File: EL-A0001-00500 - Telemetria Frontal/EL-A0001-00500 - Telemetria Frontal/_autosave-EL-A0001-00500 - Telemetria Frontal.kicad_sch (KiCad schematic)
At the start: 3 parts, among them J1 1-776087-1, U1 YAAJ_BluePill, U2 MP1584

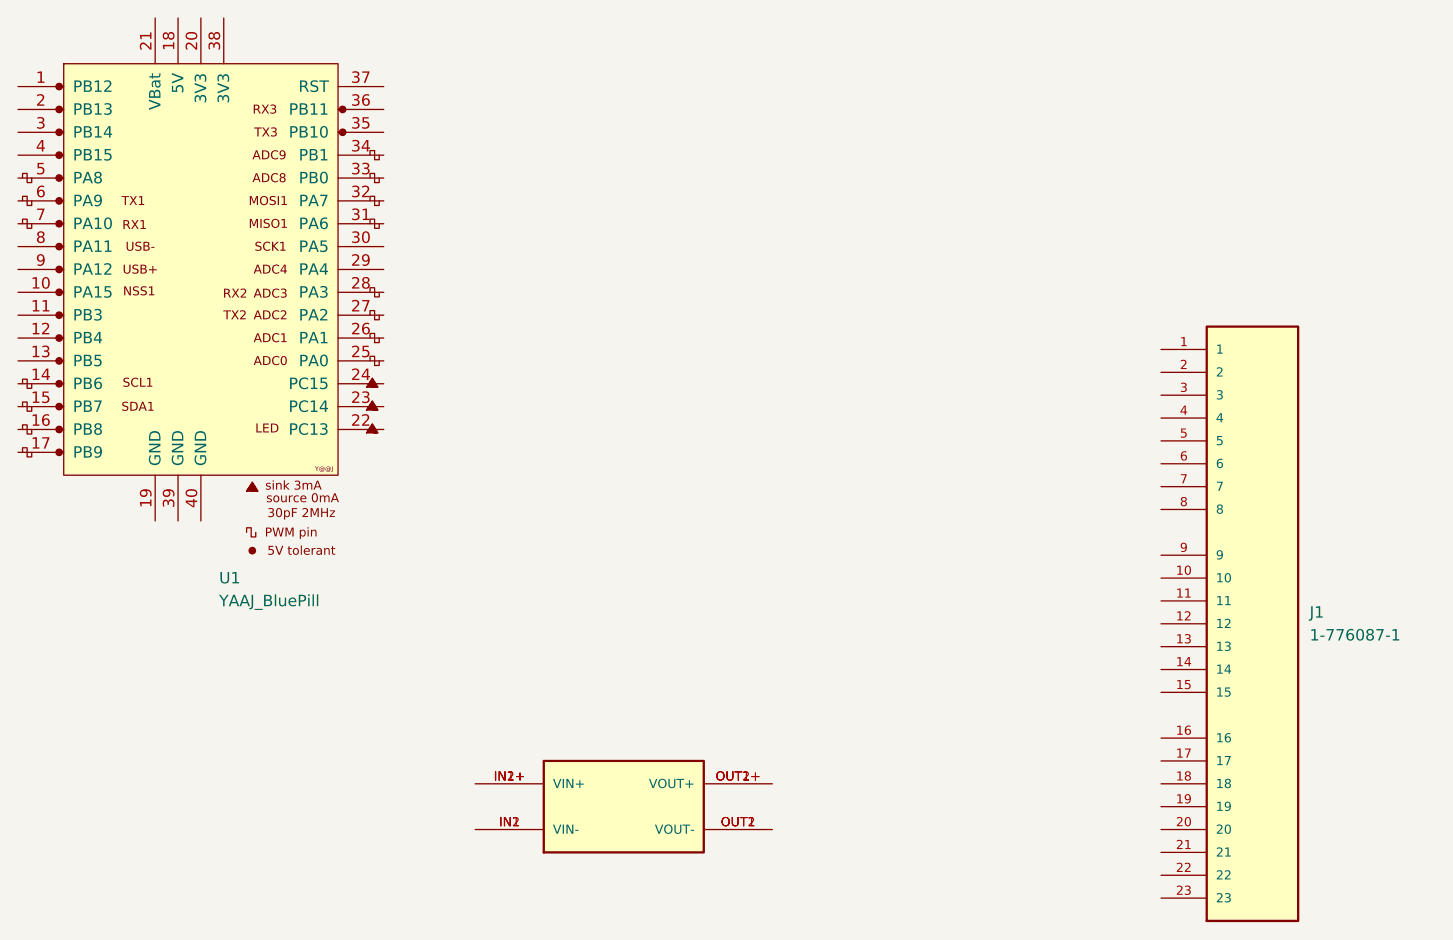
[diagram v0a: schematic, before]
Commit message: ADD: submodules
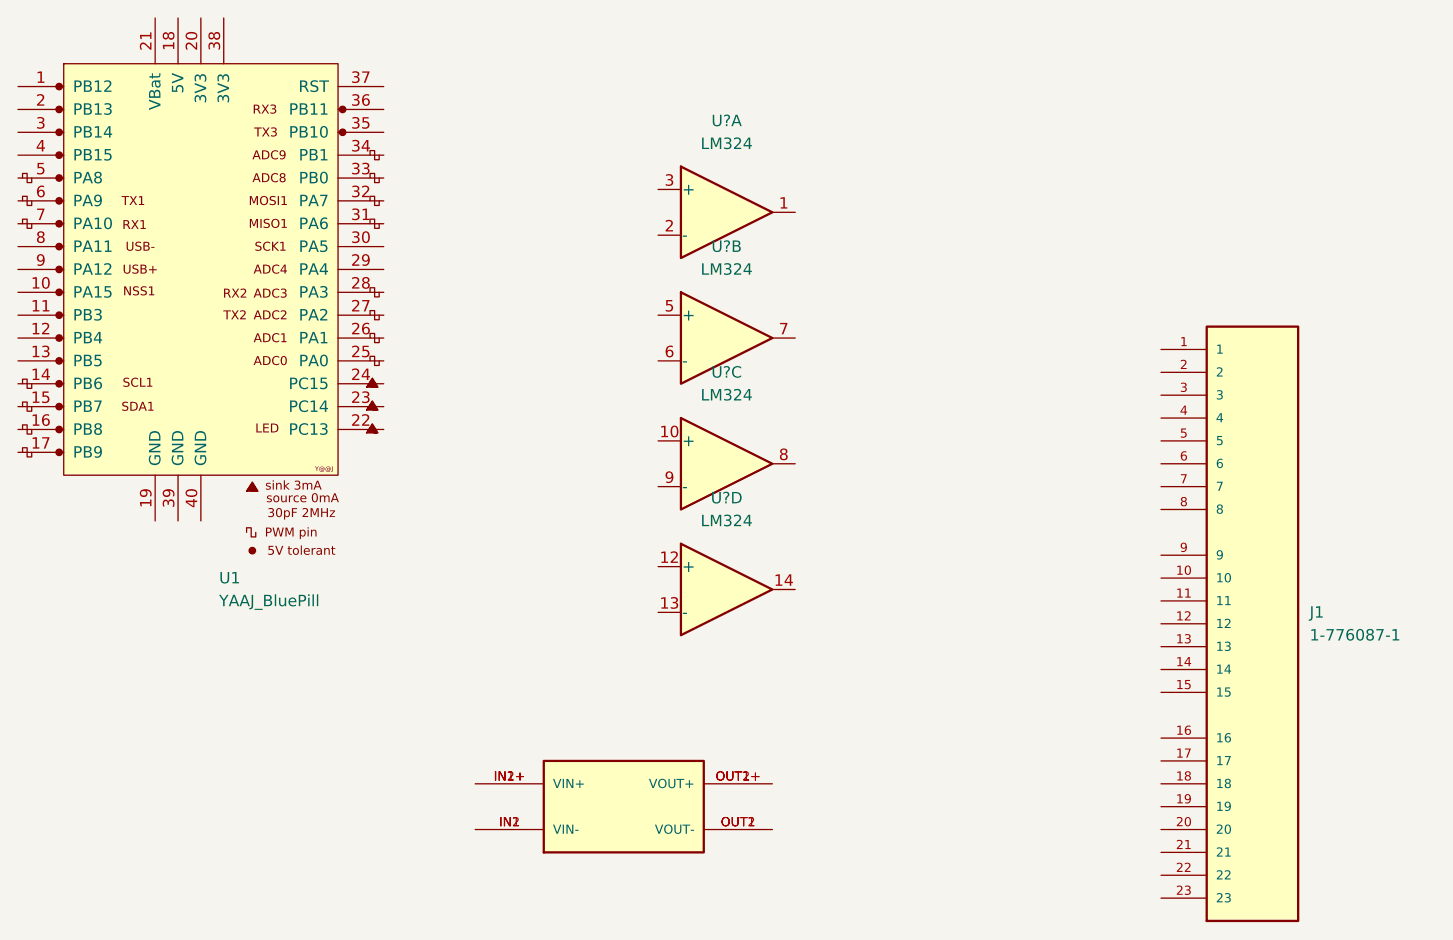
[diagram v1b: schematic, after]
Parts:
- added U? (x4): LM324, symbol Amplifier_Operational:LM324
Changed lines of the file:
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@@
 (kicad_sch (version 20211123) (generator eeschema)
   (paper "A4")
+  (symbol (lib_id "Amplifier_Operational:LM324") (at 124.46 57.15 0) (unit 1)
+    (in_bom yes) (on_board yes) (fields_autoplaced)
+    (property "Reference" "U?" (id 0) (at 124.46 46.99 0))
+    (property "Value" "LM324" (id 1) (at 124.46 49.53 0))
+    (property "Footprint" "" (id 2) (at 123.19 54.61 0)
+      (effects (font (size 1.27 1.27)) hide)
+    )
+    (property "Datasheet" "http://www.ti.com/lit/ds/symlink/lm2902-n.pdf" (id 3) (at 125.73 52.07 0)
+      (effects (font (size 1.27 1.27)) hide)
+    )
+    (pin "1")
+    (pin "2")
+    (pin "3")
+  )
   (symbol (lib_id "1-776087-1:1-776087-1") (at 182.88 102.87 0) (unit 1)
     (in_bom yes) (on_board yes) (fields_autoplaced)
@@
     (pin "9")
   )
+  (symbol (lib_id "Amplifier_Operational:LM324") (at 124.46 71.12 0) (unit 2)
+    (in_bom yes) (on_board yes) (fields_autoplaced)
+    (property "Reference" "U?" (id 0) (at 124.46 60.96 0))
+    (property "Value" "LM324" (id 1) (at 124.46 63.5 0))
+    (property "Footprint" "" (id 2) (at 123.19 68.58 0)
+      (effects (font (size 1.27 1.27)) hide)
+    )
+    (property "Datasheet" "http://www.ti.com/lit/ds/symlink/lm2902-n.pdf" (id 3) (at 125.73 66.04 0)
+      (effects (font (size 1.27 1.27)) hide)
+    )
+    (pin "5")
+    (pin "6")
+    (pin "7")
+  )
+  (symbol (lib_id "Amplifier_Operational:LM324") (at 124.46 85.09 0) (unit 3)
+    (in_bom yes) (on_board yes) (fields_autoplaced)
+    (property "Reference" "U?" (id 0) (at 124.46 74.93 0))
+    (property "Value" "LM324" (id 1) (at 124.46 77.47 0))
+    (property "Footprint" "" (id 2) (at 123.19 82.55 0)
+      (effects (font (size 1.27 1.27)) hide)
+    )
+    (property "Datasheet" "http://www.ti.com/lit/ds/symlink/lm2902-n.pdf" (id 3) (at 125.73 80.01 0)
+      (effects (font (size 1.27 1.27)) hide)
+    )
+    (pin "10")
+    (pin "8")
+    (pin "9")
+  )
+  (symbol (lib_id "Amplifier_Operational:LM324") (at 124.46 99.06 0) (unit 4)
+    (in_bom yes) (on_board yes) (fields_autoplaced)
+    (property "Reference" "U?" (id 0) (at 124.46 88.9 0))
+    (property "Value" "LM324" (id 1) (at 124.46 91.44 0))
+    (property "Footprint" "" (id 2) (at 123.19 96.52 0)
+      (effects (font (size 1.27 1.27)) hide)
+    )
+    (property "Datasheet" "http://www.ti.com/lit/ds/symlink/lm2902-n.pdf" (id 3) (at 125.73 93.98 0)
+      (effects (font (size 1.27 1.27)) hide)
+    )
+    (pin "12")
+    (pin "13")
+    (pin "14")
+  )
   (symbol (lib_id "MP1584:MP1584") (at 111.76 123.19 0) (unit 1)
     (in_bom yes) (on_board yes) (fields_autoplaced)
@@
       (reference "U2") (unit 1) (value "MP1584") (footprint "MP1584:DC-BRICK")
     )
-  )
+    (path "/2aff3e19-72c1-4135-a3b2-de43d3a56a9c"
+      (reference "U?") (unit 1) (value "LM324") (footprint "")
+    )
+    (path "/ba775785-8bac-465f-9c4f-420dafb11e9d"
+      (reference "U?") (unit 2) (value "LM324") (footprint "")
+    )
+    (path "/c0fe2b63-3553-4f3d-b46a-4fab52b073bc"
+      (reference "U?") (unit 3) (value "LM324") (footprint "")
+    )
+    (path "/c284f113-28dd-4073-a844-cc08da93adeb"
+      (reference "U?") (unit 4) (value "LM324") (footprint "")
+    )
+  )
